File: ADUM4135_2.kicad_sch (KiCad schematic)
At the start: 36 parts, among them Q5 MJD44H11T4G, Q6 MJD45H11T4G, Q7 MJD44H11T4G, Q8 MJD45H11T4G

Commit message: Добавил названия элементов в схеме
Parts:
- D19, D20: value BZT52C10-7-F -> MMSZ5240B
- D21, D22: value US3M-13 -> MURS360T3G
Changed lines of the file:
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@@
       (effects (font (size 1.27 1.27)) (justify left))
     )
-    (property "Value" "BZT52C10-7-F" (id 1) (at 111.506 80.264 90)
+    (property "Value" "MMSZ5240B" (id 1) (at 111.506 80.264 90)
       (effects (font (size 1.27 1.27)) (justify left) hide)
     )
@@
     (in_bom yes) (on_board yes)
     (property "Reference" "D21" (id 0) (at 120.142 80.264 90))
-    (property "Value" "US3M-13" (id 1) (at 115.316 81.026 0)
+    (property "Value" "MURS360T3G" (id 1) (at 115.316 81.026 0)
       (effects (font (size 1.27 1.27)) hide)
     )
@@
     (in_bom yes) (on_board yes)
     (property "Reference" "D22" (id 0) (at 126.492 145.796 0))
-    (property "Value" "US3M-13" (id 1) (at 127.254 150.622 0))
+    (property "Value" "MURS360T3G" (id 1) (at 127.254 150.622 0))
     (property "Footprint" "Diode_SMD:D_SMC" (id 2) (at 126.492 148.082 90)
       (effects (font (size 1.27 1.27)) hide)
@@
       (effects (font (size 1.27 1.27)) (justify left))
     )
-    (property "Value" "BZT52C10-7-F" (id 1) (at 110.998 159.258 0)
-      (effects (font (size 1.27 1.27)) (justify left))
-    )
+    (property "Value" "MMSZ5240B" (id 1) (at 110.998 159.258 0)
+      (effects (font (size 1.27 1.27)) (justify left))
+    )

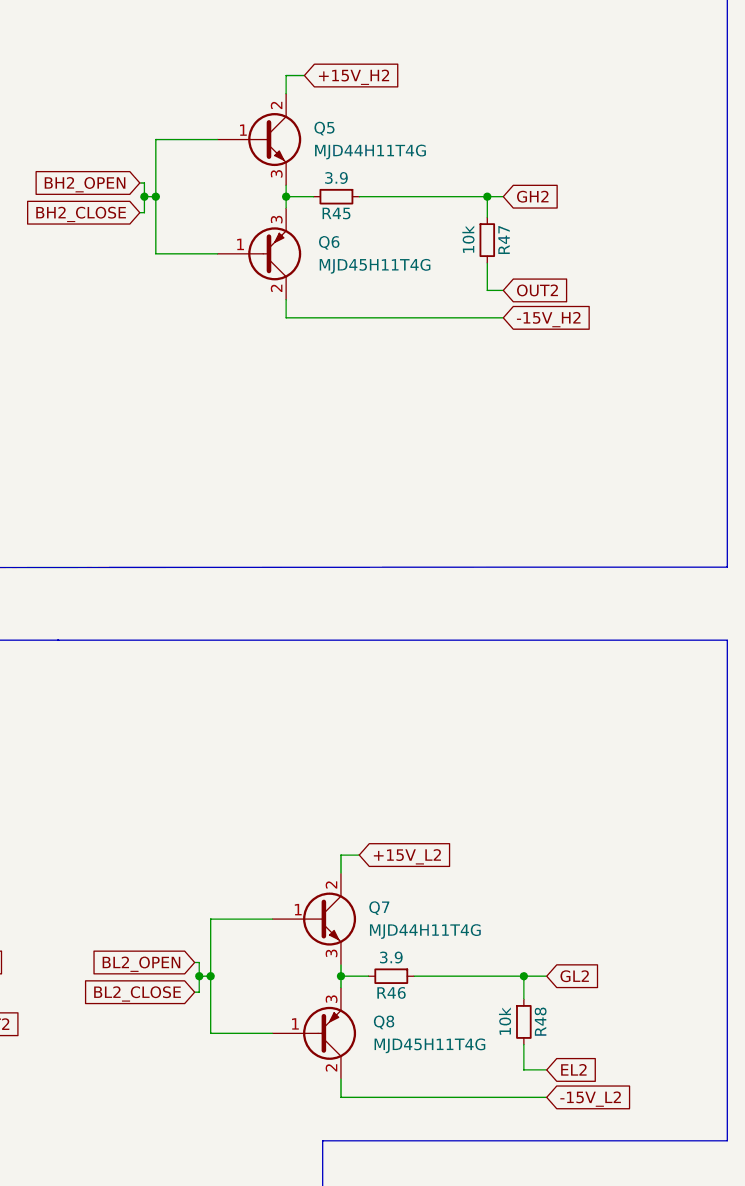
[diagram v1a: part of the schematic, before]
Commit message: Исправил ошибки, добавил резисторы в затвор, ревизия 2.0
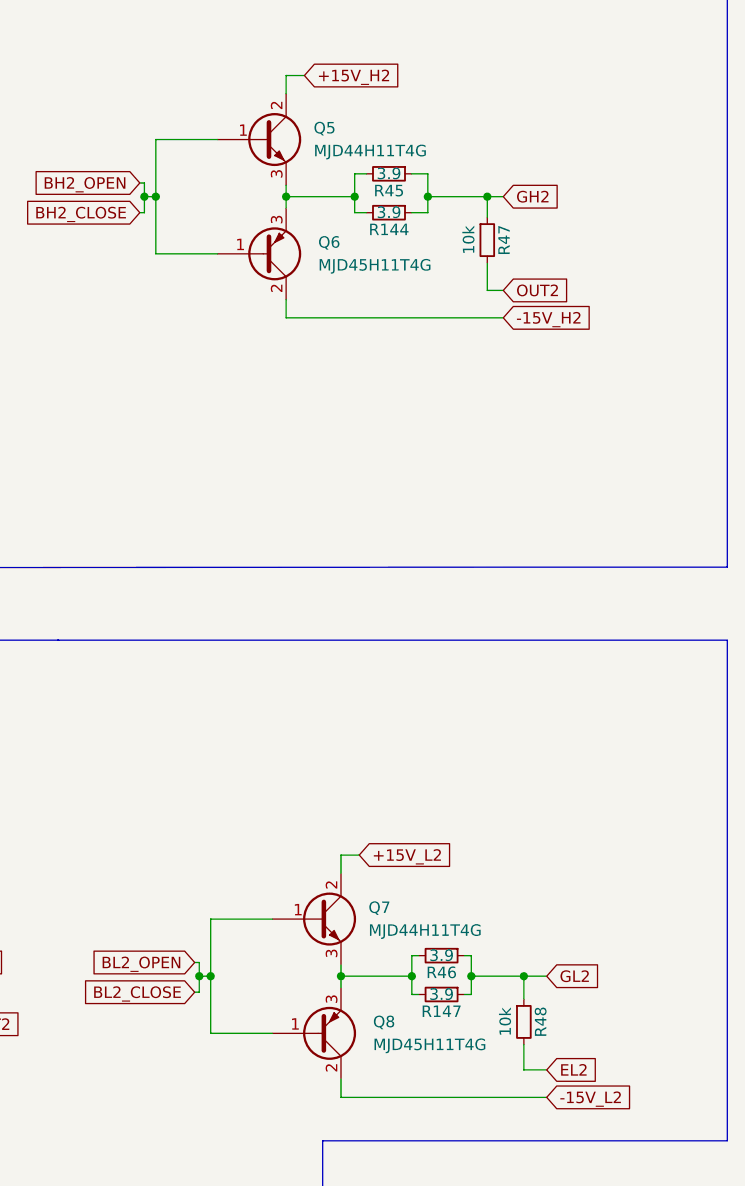
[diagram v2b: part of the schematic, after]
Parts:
- added R144, R147: 3.9, Resistor_SMD:R_2512_6332Metric_Pad1.40x3.35mm_HandSolder, symbol Device:R_Small
- R35, R36, R37, R38: footprint Resistor_SMD:R_2512_6332Metric_Pad1.40x3.35mm_HandSolder -> Resistor_SMD:R_1210_3225Metric_Pad1.30x2.65mm_HandSolder
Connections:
- net GH2: now also R144.1
- net GL2: now also R147.1
- net at Q7.3 (E), Q8.3 (E), R46.2: now also R147.2
- net at Q5.3 (E), Q6.3 (E), R45.2: now also R144.2
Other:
- moved on the sheet: R45, R46

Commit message: Версия для резонита REV2.1
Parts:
- removed R42, R44: 2.2k, Resistor_SMD:R_0805_2012Metric_Pad1.20x1.40mm_HandSolder, symbol Device:R_Small
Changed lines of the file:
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@@
   (junction (at 107.696 83.058) (diameter 0) (color 0 0 0 0)
-  )
-  (junction (at 117.856 62.992) (diameter 0) (color 0 0 0 0)
   )
   (junction (at 110.236 156.718) (diameter 0) (color 0 0 0 0)
@@
     (stroke (width 0) (type default) (color 0 0 0 0))
   )
-  (wire (pts (xy 110.236 143.256) (xy 110.236 148.082))
-    (stroke (width 0) (type default) (color 0 0 0 0))
-  )
   (wire (pts (xy 153.416 49.784) (xy 153.416 56.134))
     (stroke (width 0) (type default) (color 0 0 0 0))
@@
     (stroke (width 0) (type default) (color 0 0 0 0))
   )
-  (wire (pts (xy 113.284 143.256) (xy 113.284 141.224))
-    (stroke (width 0) (type default) (color 0 0 0 0))
-  )
   (wire (pts (xy 159.512 136.398) (xy 159.512 142.748))
     (stroke (width 0) (type default) (color 0 0 0 0))
@@
     (stroke (width 0) (type default) (color 0 0 0 0))
   )
-  (wire (pts (xy 126.492 62.992) (xy 117.856 62.992))
-    (stroke (width 0) (type default) (color 0 0 0 0))
-  )
   (wire (pts (xy 173.99 156.21) (xy 196.85 156.21))
     (stroke (width 0) (type default) (color 0 0 0 0))
@@
     (stroke (width 0) (type default) (color 0 0 0 0))
   )
-  (wire (pts (xy 123.444 141.224) (xy 126.238 141.224))
-    (stroke (width 0) (type default) (color 0 0 0 0))
-  )
   (wire (pts (xy 63.246 62.992) (xy 71.12 62.992))
     (stroke (width 0) (type default) (color 0 0 0 0))
@@
     (stroke (width 0) (type default) (color 0 0 0 0))
   )
-  (wire (pts (xy 126.492 77.216) (xy 126.492 80.01))
-    (stroke (width 0) (type default) (color 0 0 0 0))
-  )
   (wire (pts (xy 157.734 141.224) (xy 158.242 141.224))
     (stroke (width 0) (type default) (color 0 0 0 0))
@@
     (stroke (width 0) (type default) (color 0 0 0 0))
   )
-  (wire (pts (xy 113.284 141.224) (xy 118.364 141.224))
-    (stroke (width 0) (type default) (color 0 0 0 0))
-  )
   (wire (pts (xy 94.996 151.892) (xy 99.06 151.892))
     (stroke (width 0) (type default) (color 0 0 0 0))
@@
     (stroke (width 0) (type default) (color 0 0 0 0))
   )
-  (wire (pts (xy 113.284 143.256) (xy 110.236 143.256))
-    (stroke (width 0) (type default) (color 0 0 0 0))
-  )
   (wire (pts (xy 160.274 62.484) (xy 153.416 62.484))
     (stroke (width 0) (type default) (color 0 0 0 0))
   )
   (wire (pts (xy 166.37 136.398) (xy 159.512 136.398))
-    (stroke (width 0) (type default) (color 0 0 0 0))
-  )
-  (wire (pts (xy 126.492 72.136) (xy 126.492 62.992))
     (stroke (width 0) (type default) (color 0 0 0 0))
   )
@@
     )
   )
-  (global_label "+15V_H2" (shape input) (at 126.492 80.01 270) (fields_autoplaced)
-    (effects (font (size 1.27 1.27)) (justify right))
-    (property "Intersheet References" "${INTERSHEET_REFS}" (id 0) (at 126.4126 91.0107 90)
-      (effects (font (size 1.27 1.27)) (justify right) hide)
-    )
-  )
   (global_label "-15V_L2" (shape input) (at 196.85 156.21 0) (fields_autoplaced)
     (effects (font (size 1.27 1.27)) (justify left))
@@
     (effects (font (size 1.27 1.27)) (justify left))
     (property "Intersheet References" "${INTERSHEET_REFS}" (id 0) (at 110.3147 66.7226 0)
-      (effects (font (size 1.27 1.27)) (justify left) hide)
-    )
-  )
-  (global_label "+15V_L2" (shape input) (at 126.238 141.224 0) (fields_autoplaced)
-    (effects (font (size 1.27 1.27)) (justify left))
-    (property "Intersheet References" "${INTERSHEET_REFS}" (id 0) (at 136.9363 141.1446 0)
       (effects (font (size 1.27 1.27)) (justify left) hide)
     )
@@
     (pin "1")
   )
-  (symbol (lib_id "Device:R_Small") (at 120.904 141.224 90) (unit 1)
-    (in_bom yes) (on_board yes)
-    (property "Reference" "R42" (id 0) (at 120.904 139.192 90))
-    (property "Value" "2.2k" (id 1) (at 120.904 143.256 90))
-    (property "Footprint" "Resistor_SMD:R_0805_2012Metric_Pad1.20x1.40mm_HandSolder" (id 2) (at 120.904 141.224 0)
-      (effects (font (size 1.27 1.27)) hide)
-    )
-    (property "Datasheet" "~" (id 3) (at 120.904 141.224 0)
-      (effects (font (size 1.27 1.27)) hide)
-    )
-    (pin "1")
-    (pin "2")
-  )
   (symbol (lib_id "Device:D_Small") (at 117.856 80.264 90) (unit 1)
     (in_bom yes) (on_board yes)
@@
       (effects (font (size 1.27 1.27)) hide)
     )
-    (pin "1")
-    (pin "2")
-  )
-  (symbol (lib_id "Device:R_Small") (at 126.492 74.676 0) (unit 1)
-    (in_bom yes) (on_board yes)
-    (property "Reference" "R44" (id 0) (at 128.524 74.676 0))
-    (property "Value" "2.2k" (id 1) (at 124.46 74.676 90))
-    (property "Footprint" "Resistor_SMD:R_0805_2012Metric_Pad1.20x1.40mm_HandSolder" (id 2) (at 126.492 74.676 0)
-      (effects (font (size 1.27 1.27)) hide)
-    )
-    (property "Datasheet" "~" (id 3) (at 126.492 74.676 0)
-      (effects (font (size 1.27 1.27)) hide)
-    )

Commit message: Финальная версия для производства
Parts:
- R144, R147, R45, R46: value 3.9 -> 3
- R35, R36, R37, R38: value 3.9 -> 50
- R41, R43: value 0 -> 10k
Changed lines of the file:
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@@
     (in_bom yes) (on_board yes)
     (property "Reference" "R37" (id 0) (at 97.79 49.657 90))
-    (property "Value" "3.9" (id 1) (at 97.79 45.72 90))
+    (property "Value" "50" (id 1) (at 97.79 45.72 90))
     (property "Footprint" "Resistor_SMD:R_1210_3225Metric_Pad1.30x2.65mm_HandSolder" (id 2) (at 97.79 47.752 0)
       (effects (font (size 1.27 1.27)) hide)
@@
     (in_bom yes) (on_board yes)
     (property "Reference" "R38" (id 0) (at 97.79 57.277 90))
-    (property "Value" "3.9" (id 1) (at 97.79 53.34 90))
+    (property "Value" "50" (id 1) (at 97.79 53.34 90))
     (property "Footprint" "Resistor_SMD:R_1210_3225Metric_Pad1.30x2.65mm_HandSolder" (id 2) (at 97.79 55.372 0)
       (effects (font (size 1.27 1.27)) hide)
@@
     (in_bom yes) (on_board yes)
     (property "Reference" "D22" (id 0) (at 126.492 145.796 0))
-    (property "Value" "MURS360T3G" (id 1) (at 127.254 150.622 0))
+    (property "Value" "MURS360T3G" (id 1) (at 130.048 150.622 0))
     (property "Footprint" "Diode_SMD:D_SMC" (id 2) (at 126.492 148.082 90)
       (effects (font (size 1.27 1.27)) hide)
@@
     (in_bom yes) (on_board yes)
     (property "Reference" "R43" (id 0) (at 120.904 145.796 90))
-    (property "Value" "0" (id 1) (at 120.904 150.622 90))
+    (property "Value" "10k" (id 1) (at 120.904 150.622 90))
     (property "Footprint" "Resistor_SMD:R_1206_3216Metric_Pad1.30x1.75mm_HandSolder" (id 2) (at 120.904 148.082 0)
       (effects (font (size 1.27 1.27)) hide)
@@
     (in_bom yes) (on_board yes)
     (property "Reference" "R45" (id 0) (at 179.324 55.499 90))
-    (property "Value" "3.9" (id 1) (at 179.324 53.594 90))
+    (property "Value" "3" (id 1) (at 179.324 53.594 90))
     (property "Footprint" "Resistor_SMD:R_2512_6332Metric_Pad1.40x3.35mm_HandSolder" (id 2) (at 179.324 53.594 0)
       (effects (font (size 1.27 1.27)) hide)
@@
     (in_bom yes) (on_board yes)
     (property "Reference" "R144" (id 0) (at 179.324 59.817 90))
-    (property "Value" "3.9" (id 1) (at 179.324 57.912 90))
+    (property "Value" "3" (id 1) (at 179.324 57.912 90))
     (property "Footprint" "Resistor_SMD:R_2512_6332Metric_Pad1.40x3.35mm_HandSolder" (id 2) (at 179.324 57.912 0)
       (effects (font (size 1.27 1.27)) hide)
@@
     (in_bom yes) (on_board yes)
     (property "Reference" "R147" (id 0) (at 185.166 146.685 90))
-    (property "Value" "3.9" (id 1) (at 185.166 144.78 90))
+    (property "Value" "3" (id 1) (at 185.166 144.78 90))
     (property "Footprint" "Resistor_SMD:R_2512_6332Metric_Pad1.40x3.35mm_HandSolder" (id 2) (at 185.166 144.78 0)
       (effects (font (size 1.27 1.27)) hide)
@@
     (in_bom yes) (on_board yes)
     (property "Reference" "R35" (id 0) (at 97.536 134.747 90))
-    (property "Value" "3.9" (id 1) (at 97.536 130.81 90))
+    (property "Value" "50" (id 1) (at 97.536 130.81 90))
     (property "Footprint" "Resistor_SMD:R_1210_3225Metric_Pad1.30x2.65mm_HandSolder" (id 2) (at 97.536 132.842 0)
       (effects (font (size 1.27 1.27)) hide)
@@
     (in_bom yes) (on_board yes)
     (property "Reference" "R46" (id 0) (at 185.166 142.367 90))
-    (property "Value" "3.9" (id 1) (at 185.166 140.462 90))
+    (property "Value" "3" (id 1) (at 185.166 140.462 90))
     (property "Footprint" "Resistor_SMD:R_2512_6332Metric_Pad1.40x3.35mm_HandSolder" (id 2) (at 185.166 140.462 0)
       (effects (font (size 1.27 1.27)) hide)
@@
     (in_bom yes) (on_board yes)
     (property "Reference" "R41" (id 0) (at 120.142 74.676 0))
-    (property "Value" "0" (id 1) (at 115.824 74.676 90))
+    (property "Value" "10k" (id 1) (at 115.824 74.676 90))
     (property "Footprint" "Resistor_SMD:R_1206_3216Metric_Pad1.30x1.75mm_HandSolder" (id 2) (at 117.856 74.676 0)
       (effects (font (size 1.27 1.27)) hide)
@@
     (in_bom yes) (on_board yes)
     (property "Reference" "R36" (id 0) (at 97.536 142.367 90))
-    (property "Value" "3.9" (id 1) (at 97.536 138.43 90))
+    (property "Value" "50" (id 1) (at 97.536 138.43 90))
     (property "Footprint" "Resistor_SMD:R_1210_3225Metric_Pad1.30x2.65mm_HandSolder" (id 2) (at 97.536 140.462 0)
       (effects (font (size 1.27 1.27)) hide)
